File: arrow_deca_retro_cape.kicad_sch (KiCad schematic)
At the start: 74 parts, among them J1 DB15_Female_HighDensity_Mount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, J10 Conn_02x06_Odd_Even, J11 PMOD1, J12 PMOD2, J14 Conn_01x02, J15 Conn_01x03, J16 Conn_01x06, J17 Conn_01x02, J18 Conn_01x03, J19 DINC_MIN_TM_6_1, J20 PMOD3, J21 USB3_A, J22 Conn_01x03, J3 Conn_01x06, J4 DB9_Male_MountingHoles, J5 DINC_MIN_TM_6_1, J6 Conn_02x20_Odd_Even, J7 Conn_01x03, J8 P8_Male, J9 P9_Male, U4 LM1117-3.3, U5 LM1117-2.5

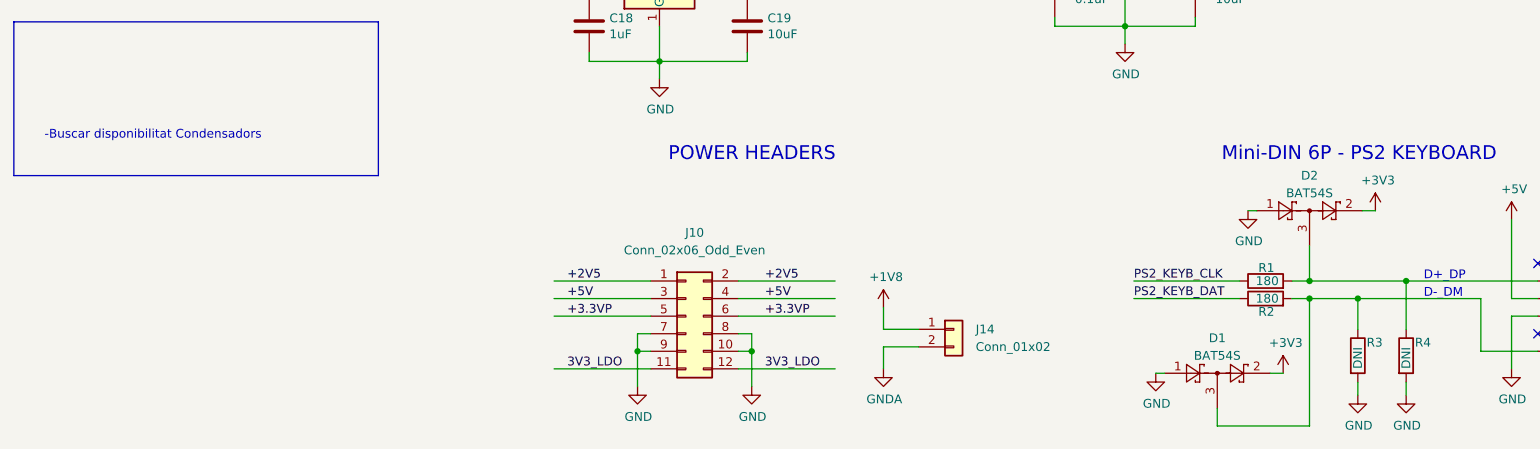
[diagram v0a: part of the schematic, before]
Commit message: updated status. received pcb. started testing
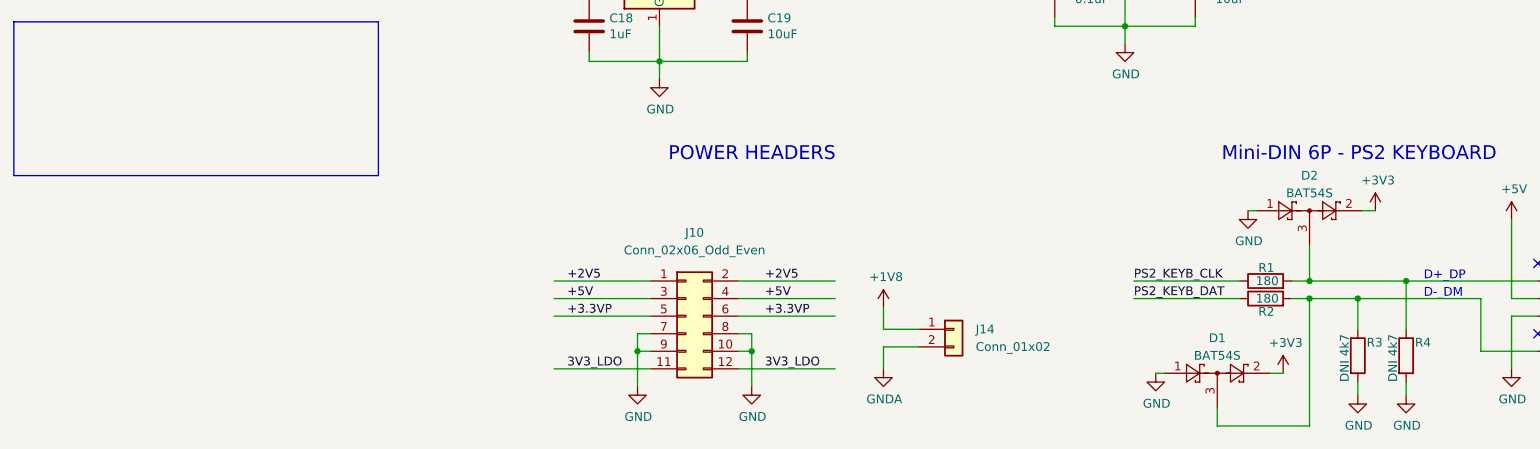
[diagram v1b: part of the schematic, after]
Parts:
- R3, R4: value DNI -> DNI 4k7
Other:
- note removed: "-Buscar disponibilitat Condensadors"
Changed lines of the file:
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@@
     (effects (font (size 2 2)) (justify left bottom))
   )
-  (text "-Buscar disponibilitat Condensadors\n" (at -52.705 240.03 0)
-    (effects (font (size 1.27 1.27)) (justify left bottom))
-  )
   (text "DETO PMOD (6 pin)" (at 33.02 151.765 0)
     (effects (font (size 2 2)) (justify left bottom))
@@
       (effects (font (size 1.27 1.27)) (justify left))
     )
-    (property "Value" "DNI" (id 1) (at 144.145 273.05 90)
+    (property "Value" "DNI 4k7" (id 1) (at 142.24 274.955 90)
       (effects (font (size 1.27 1.27)) (justify left))
     )
@@
       (effects (font (size 1.27 1.27)) (justify left))
     )
-    (property "Value" "DNI" (id 1) (at 137.16 273.05 90)
+    (property "Value" "DNI 4k7" (id 1) (at 135.255 274.955 90)
       (effects (font (size 1.27 1.27)) (justify left))
     )
@@
     )
     (path "/4e409b81-c5d2-42ba-af6f-8fc2e29e95fa"
-      (reference "R3") (unit 1) (value "DNI") (footprint "Resistor_SMD:R_0805_2012Metric_Pad1.20x1.40mm_HandSolder")
+      (reference "R3") (unit 1) (value "DNI 4k7") (footprint "Resistor_SMD:R_0805_2012Metric_Pad1.20x1.40mm_HandSolder")
     )
     (path "/1eb0fb7c-0c77-4e19-890a-f328471d6c6d"
-      (reference "R4") (unit 1) (value "DNI") (footprint "Resistor_SMD:R_0805_2012Metric_Pad1.20x1.40mm_HandSolder")
+      (reference "R4") (unit 1) (value "DNI 4k7") (footprint "Resistor_SMD:R_0805_2012Metric_Pad1.20x1.40mm_HandSolder")
     )
     (path "/9167d64e-691b-49d2-aa0b-617b235bc81c"

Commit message: v0.72 updated readme and pinout spreadsheet
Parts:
- removed J3: Conn_01x06, Connector_PinHeader_2.54mm:PinHeader_1x06_P2.54mm_Vertical, symbol Connector_Generic:Conn_01x06
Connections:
- net JOY_MUX_DETO3 renamed DETO3_JOY_MUX
- net SPI_CS_FPGA renamed SPI_CS2
- net SPI_CS_IO renamed SPI_CS1
- net SPI_CS_OSD renamed SPI_CS0_CLKBD
- net SPI_DI (MISO) renamed SPI_MISO_WSDB
- net SPI_DO (MOSI) renamed SPI_MOSI
- net SPI_SCK renamed SPI_SCLK_DABD
- no-connect marks 10 -> 9
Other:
- note added: "(DI)"
- note added: "(DO)"
- note removed: "3V3"
- note removed: "JTAG (Pogo pins)"
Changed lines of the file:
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@@
   (no_connect (at 222.885 173.355))
   (no_connect (at 222.885 158.115))
-  (no_connect (at 95.25 163.195))
   (no_connect (at 163.195 257.81))
   (no_connect (at 257.175 267.97))
@@
     (stroke (width 0) (type default) (color 0 0 0 0))
   )
-  (wire (pts (xy 95.25 165.735) (xy 78.74 165.735))
-    (stroke (width 0) (type default) (color 0 0 0 0))
-  )
   (wire (pts (xy 173.355 193.675) (xy 181.61 193.675))
     (stroke (width 0) (type default) (color 0 0 0 0))
@@
     (stroke (width 0) (type default) (color 0 0 0 0))
   )
-  (wire (pts (xy 95.25 168.275) (xy 78.74 168.275))
-    (stroke (width 0) (type default) (color 0 0 0 0))
-  )
   (wire (pts (xy 378.46 63.5) (xy 361.95 63.5))
     (stroke (width 0) (type default) (color 0 0 0 0))
@@
     (stroke (width 0) (type default) (color 0 0 0 0))
   )
-  (wire (pts (xy 95.25 173.355) (xy 78.74 173.355))
-    (stroke (width 0) (type default) (color 0 0 0 0))
-  )
   (wire (pts (xy 36.195 223.52) (xy 36.195 228.6))
     (stroke (width 0) (type default) (color 0 0 0 0))
@@
     (stroke (width 0) (type default) (color 0 0 0 0))
   )
-  (wire (pts (xy 91.44 179.07) (xy 91.44 175.895))
-    (stroke (width 0) (type default) (color 0 0 0 0))
-  )
   (wire (pts (xy 47.625 273.05) (xy 61.595 273.05))
     (stroke (width 0) (type default) (color 0 0 0 0))
@@
     (stroke (width 0) (type default) (color 0 0 0 0))
   )
-  (wire (pts (xy 95.25 170.815) (xy 78.74 170.815))
-    (stroke (width 0) (type default) (color 0 0 0 0))
-  )
   (wire (pts (xy 132.08 42.545) (xy 115.57 42.545))
     (stroke (width 0) (type default) (color 0 0 0 0))
@@
     (stroke (width 0) (type default) (color 0 0 0 0))
   )
-  (wire (pts (xy 91.44 175.895) (xy 95.25 175.895))
-    (stroke (width 0) (type default) (color 0 0 0 0))
-  )
   (wire (pts (xy 346.075 193.675) (xy 361.95 193.675))
     (stroke (width 0) (type default) (color 0 0 0 0))
@@
     (effects (font (size 1.27 1.27)) (justify left bottom))
   )
-  (text "JTAG (Pogo pins)" (at 81.915 151.765 0)
-    (effects (font (size 2 2)) (justify left bottom))
-  )
   (text "POWER HEADERS" (at 37.465 243.205 0)
     (effects (font (size 2 2)) (justify left bottom))
@@
     (effects (font (size 2 2)) (justify left bottom))
   )
-  (text "3V3" (at 88.9 163.83 0)
-    (effects (font (size 1.27 1.27)) (justify left bottom))
-  )
   (text "LRCLK" (at 25.4 169.545 0)
     (effects (font (size 1.27 1.27)) (justify left bottom))
@@
     (effects (font (size 2 2)) (justify left bottom))
   )
+  (text "(DI)" (at 228.6 93.345 0)
+    (effects (font (size 1.27 1.27)) (justify left bottom))
+  )
   (text "AIN0" (at 31.75 85.725 0)
     (effects (font (size 1.27 1.27)) (justify left bottom))
@@
     (effects (font (size 2 2)) (justify left bottom))
   )
+  (text "(DO)" (at 228.6 90.805 0)
+    (effects (font (size 1.27 1.27)) (justify left bottom))
+  )
   (text "EXTERNAL MISTER MODULE" (at 336.55 21.59 0)
     (effects (font (size 2 2)) (justify left bottom))
@@
     (effects (font (size 1.27 1.27)) (justify left bottom))
   )
-  (label "SPI_DI (MISO)" (at 38.1 73.025 0)
+  (label "SPI_MISO_WSDB" (at 38.1 73.025 0)
     (effects (font (size 1.27 1.27)) (justify left bottom))
   )
@@
     (effects (font (size 1.27 1.27)) (justify left bottom))
   )
-  (label "TMS" (at 78.74 168.275 0)
-    (effects (font (size 1.27 1.27)) (justify left bottom))
-  )
   (label "DQ6" (at 118.11 50.165 0)
     (effects (font (size 1.27 1.27)) (justify left bottom))
@@
     (effects (font (size 1.27 1.27)) (justify left bottom))
   )
-  (label "JOY_MUX_DETO3" (at 255.905 203.835 0)
+  (label "DETO3_JOY_MUX" (at 255.905 203.835 0)
     (effects (font (size 1.27 1.27)) (justify left bottom))
   )
@@
     (effects (font (size 1.27 1.27)) (justify left bottom))
   )
-  (label "SPI_CS_IO" (at 153.67 40.005 0)
+  (label "SPI_CS1" (at 153.67 40.005 0)
     (effects (font (size 1.27 1.27)) (justify left bottom))
   )
-  (label "JOY_MUX_DETO3" (at 38.1 88.265 0)
+  (label "DETO3_JOY_MUX" (at 38.1 88.265 0)
     (effects (font (size 1.27 1.27)) (justify left bottom))
   )
@@
     (effects (font (size 1.27 1.27)) (justify left bottom))
   )
-  (label "JOY_MUX_DETO3" (at 32.385 167.005 0)
+  (label "DETO3_JOY_MUX" (at 32.385 167.005 0)
     (effects (font (size 1.27 1.27)) (justify left bottom))
   )
@@
     (effects (font (size 1.27 1.27)) (justify left bottom))
   )
-  (label "TDI" (at 78.74 165.735 0)
-    (effects (font (size 1.27 1.27)) (justify left bottom))
-  )
   (label "A7" (at 336.55 58.42 0)
     (effects (font (size 1.27 1.27)) (justify left bottom))
@@
     (effects (font (size 1.27 1.27)) (justify left bottom))
   )
-  (label "SPI_CS_OSD" (at 217.805 88.265 0)
+  (label "SPI_CS0_CLKBD" (at 213.36 88.265 0)
     (effects (font (size 1.27 1.27)) (justify left bottom))
   )
@@
     (effects (font (size 1.27 1.27)) (justify left bottom))
   )
-  (label "SPI_CS_IO" (at 254.635 93.345 0)
+  (label "SPI_CS1" (at 254.635 93.345 0)
     (effects (font (size 1.27 1.27)) (justify left bottom))
   )
@@
     (effects (font (size 1.27 1.27)) (justify left bottom))
   )
-  (label "SPI_DO (MOSI)" (at 68.58 73.025 0)
+  (label "SPI_MOSI" (at 68.58 73.025 0)
     (effects (font (size 1.27 1.27)) (justify left bottom))
   )
-  (label "SPI_DO (MOSI)" (at 217.805 90.805 0)
+  (label "SPI_MOSI" (at 213.36 90.805 0)
     (effects (font (size 1.27 1.27)) (justify left bottom))
   )
@@
     (effects (font (size 1.27 1.27)) (justify left bottom))
   )
-  (label "SPI_SCK" (at 217.805 95.885 0)
+  (label "SPI_SCLK_DABD" (at 213.36 95.885 0)
     (effects (font (size 1.27 1.27)) (justify left bottom))
   )
@@
     (effects (font (size 1.27 1.27)) (justify left bottom))
   )
-  (label "SPI_CS_OSD" (at 118.11 40.005 0)
+  (label "SPI_CS0_CLKBD" (at 118.11 40.005 0)
     (effects (font (size 1.27 1.27)) (justify left bottom))
   )
@@
     (effects (font (size 1.27 1.27)) (justify left bottom))
   )
-  (label "TDO" (at 78.74 170.815 0)
-    (effects (font (size 1.27 1.27)) (justify left bottom))
-  )
   (label "DQ8" (at 153.67 62.865 0)
     (effects (font (size 1.27 1.27)) (justify left bottom))
@@
     (effects (font (size 1.27 1.27)) (justify left bottom))
   )
-  (label "SPI_DI (MISO)" (at 217.805 93.345 0)
+  (label "SPI_MISO_WSDB" (at 213.36 93.345 0)
     (effects (font (size 1.27 1.27)) (justify left bottom))
   )
@@
     (effects (font (size 1.27 1.27)) (justify left bottom))
   )
-  (label "SPI_CS_FPGA" (at 68.58 88.265 0)
+  (label "SPI_CS2" (at 68.58 88.265 0)
     (effects (font (size 1.27 1.27)) (justify left bottom))
   )
@@
     (effects (font (size 1.27 1.27)) (justify left bottom))
   )
-  (label "TCK" (at 78.74 173.355 0)
-    (effects (font (size 1.27 1.27)) (justify left bottom))
-  )
-  (label "SPI_CS_FPGA" (at 254.635 95.885 0)
+  (label "SPI_CS2" (at 254.635 95.885 0)
     (effects (font (size 1.27 1.27)) (justify left bottom))
   )
@@
     (effects (font (size 1.27 1.27)) (justify left bottom))
   )
-  (label "SPI_SCK" (at 38.1 75.565 0)
+  (label "SPI_SCLK_DABD" (at 38.1 75.565 0)
     (effects (font (size 1.27 1.27)) (justify left bottom))
   )
@@
     (pin "3")
   )
-  (symbol (lib_id "power:GND") (at 91.44 179.07 0) (unit 1)
-    (in_bom yes) (on_board yes)
-    (property "Reference" "#PWR02" (id 0) (at 91.44 185.42 0)
-      (effects (font (size 1.27 1.27)) hide)
-    )
-    (property "Value" "GND" (id 1) (at 91.567 183.4642 0))
-    (property "Footprint" "" (id 2) (at 91.44 179.07 0)
-      (effects (font (size 1.27 1.27)) hide)
-    )
-    (property "Datasheet" "" (id 3) (at 91.44 179.07 0)
-      (effects (font (size 1.27 1.27)) hide)
-    )
-    (pin "1")
-  )
   (symbol (lib_id "Device:C") (at 113.665 218.44 0) (unit 1)
     (in_bom yes) (on_board yes)
@@
     (pin "9")
   )
-  (symbol (lib_id "Connector_Generic:Conn_01x06") (at 100.33 168.275 0) (unit 1)
-    (in_bom yes) (on_board yes) (fields_autoplaced)
-    (property "Reference" "J3" (id 0) (at 102.87 168.2749 0)
-      (effects (font (size 1.27 1.27)) (justify left))
-    )
-    (property "Value" "Conn_01x06" (id 1) (at 102.87 170.8149 0)
-      (effects (font (size 1.27 1.27)) (justify left))
-    )
-    (property "Footprint" "Connector_PinHeader_2.54mm:PinHeader_1x06_P2.54mm_Vertical" (id 2) (at 100.33 168.275 0)
-      (effects (font (size 1.27 1.27)) hide)
-    )
-    (property "Datasheet" "~" (id 3) (at 100.33 168.275 0)
-      (effects (font (size 1.27 1.27)) hide)
-    )
-    (pin "1")
-    (pin "2")
-    (pin "3")
-    (pin "4")
-    (pin "5")
-    (pin "6")
-  )
   (symbol (lib_id "Device:R") (at 169.545 149.225 90) (unit 1)
     (in_bom yes) (on_board yes)
@@
       (reference "#PWR01") (unit 1) (value "GND") (footprint "")
     )
-    (path "/aaab055d-e2c8-47ec-bf52-ba6cbf89c068"
-      (reference "#PWR02") (unit 1) (value "GND") (footprint "")
-    )
     (path "/2536e930-06a4-43c1-bb06-fbe9f6f63e41"
       (reference "#PWR03") (unit 1) (value "GND") (footprint "")
@@
       (reference "J1") (unit 1) (value "DB15_Female_HighDensity_MountingHoles") (footprint "vga:DSUB-15-HD_Female_Horizontal_P2.29x2.54mm_EdgePinOffset3.03mm_Housed_MountingHolesOffset4.94mm")
     )
-    (path "/e9a4ad61-c16f-4a36-9385-12858092576f"
-      (reference "J3") (unit 1) (value "Conn_01x06") (footprint "Connector_PinHeader_2.54mm:PinHeader_1x06_P2.54mm_Vertical")
-    )
     (path "/5d157a0f-3ba8-4d7f-8aff-9786af9f14a7"

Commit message: v0.75 see changelog
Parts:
- removed D1, D10, D11, D12, D2, D3, D4, D5, D6, D7, D8, D9: BAT54S, Package_TO_SOT_SMD:SOT-23, symbol Diode:BAT54S
- added D1, D12, D2, D3, D4: MMSZ5225BG, Diode_SMD:D_SOD-123, symbol Diode:BZT52Bxx
- added D10, D11, D5, D6, D7, D8, D9: MMSZ5221BT1G, Diode_SMD:D_SOD-123, symbol Diode:BZT52Bxx
- added JP3: (no value), symbol Jumper:SolderJumper_2_Open
- added JP4: Conn_01x02, Connector_PinHeader_2.54mm:PinHeader_1x02_P2.54mm_Vertical, symbol Connector_Generic:Conn_01x02
- J1: footprint vga:DSUB-15-HD_Female_Horizontal_P2.29x2.54mm_EdgePinOffset3.03mm_Housed_MountingHolesOffset4.94mm -> Connector_Dsub:DSUB-15-HD_Female_Horizontal_P2.29x1.98mm_EdgePinOffset3.03mm_Housed_MountingHolesOffset4.94mm
- J10: footprint Connector_PinSocket_2.54mm:PinSocket_2x06_P2.54mm_Vertical -> Connector_PinSocket_2.54mm:PinSocket_1x06_P2.54mm_Vertical; symbol Connector_Generic:Conn_02x06_Odd_Even -> Connector_Generic:Conn_01x06
- J16: footprint Connector_PinHeader_2.54mm:PinHeader_1x06_P2.54mm_Vertical -> Connector_PinSocket_2.54mm:PinSocket_1x06_P2.54mm_Vertical
- R1, R10, R11, R12, R13, R14, R15, R16, R2, R5, R6, R9: value 180 -> 510
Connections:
- net +2V5: no longer J10.2 (Pin_2)
- net +3.3VP: now also J10.4 (Pin_4); no longer J10.5 (Pin_5), J10.6 (Pin_6)
- net +5V: now also J10.2 (Pin_2), JP4.2 (Pin_2); no longer J10.3 (Pin_3), J10.4 (Pin_4)
- net 3V3_LDO: now also J10.6 (Pin_6); no longer J10.11 (Pin_11), J10.12 (Pin_12)
- net GND: now also J10.3 (Pin_3), J10.5 (Pin_5), D1.2 (A), D10.2 (A), D11.2 (A), D12.2 (A), D2.2 (A), D3.2 (A), D4.2 (A), D5.2 (A), D6.2 (A), D7.2 (A), D8.2 (A), D9.2 (A); no longer J10.10 (Pin_10), J10.7 (Pin_7), J10.8 (Pin_8), J10.9 (Pin_9)
- net JOY1_B1_P6: now also D8.1 (K)
- net JOY1_B2_P9: now also D5.1 (K)
- net JOY1_DOWN: now also D6.1 (K)
- net JOY1_LEFT: now also D9.1 (K)
- net JOY1_RIGHT: now also D7.1 (K)
- net JOY1_UP: now also D10.1 (K)
- net MUX: now also JP3.2 (B); no longer R16.2
- net PS2_KEYB_CLK: now also D1.1 (K)
- net PS2_KEYB_DAT: now also D2.1 (K)
- net PS2_MOUSE_CLK: now also D3.1 (K)
- net PS2_MOUSE_DAT: now also D4.1 (K)
- net at J1.9: now also JP4.1 (Pin_1)
- new net: JP3.1 (A), R16.2
- no-connect marks 9 -> 8
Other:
- note added: "DNI"
- moved on the sheet: C18, C19, C20, C21, J1, J12, J14, J15, J16, J18, J19, J20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

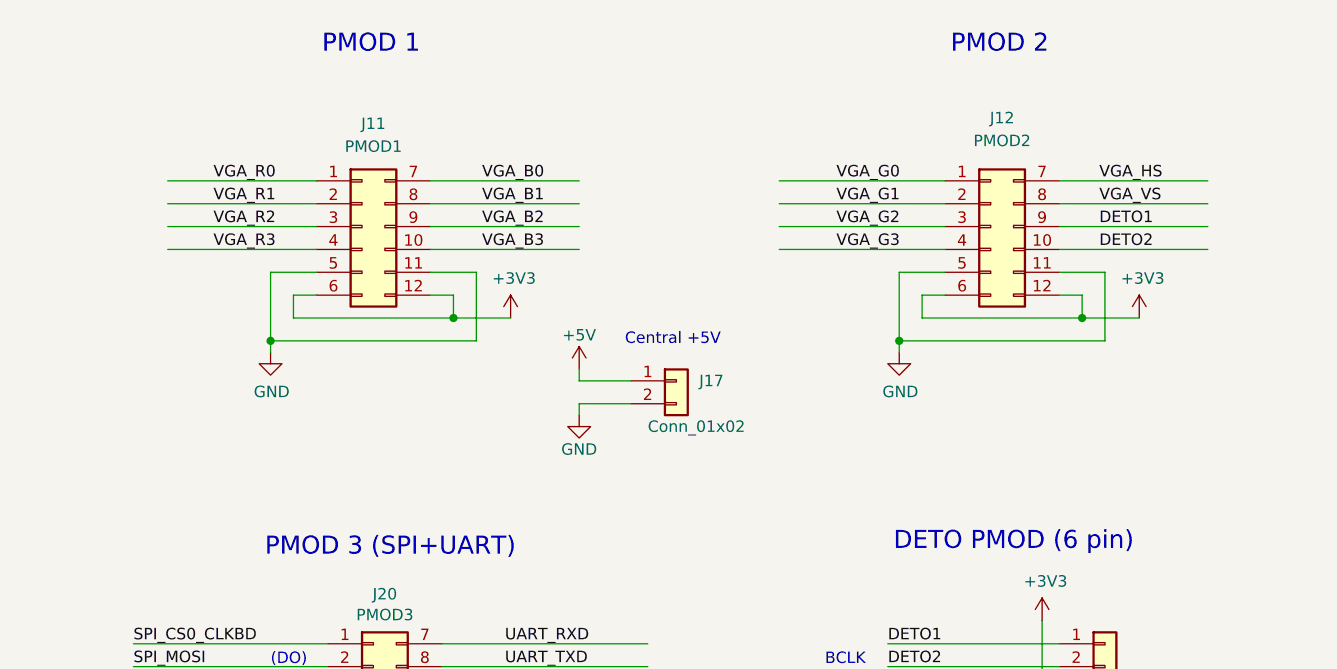
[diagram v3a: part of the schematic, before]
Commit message: v0.76 double pmod added 4 central pins
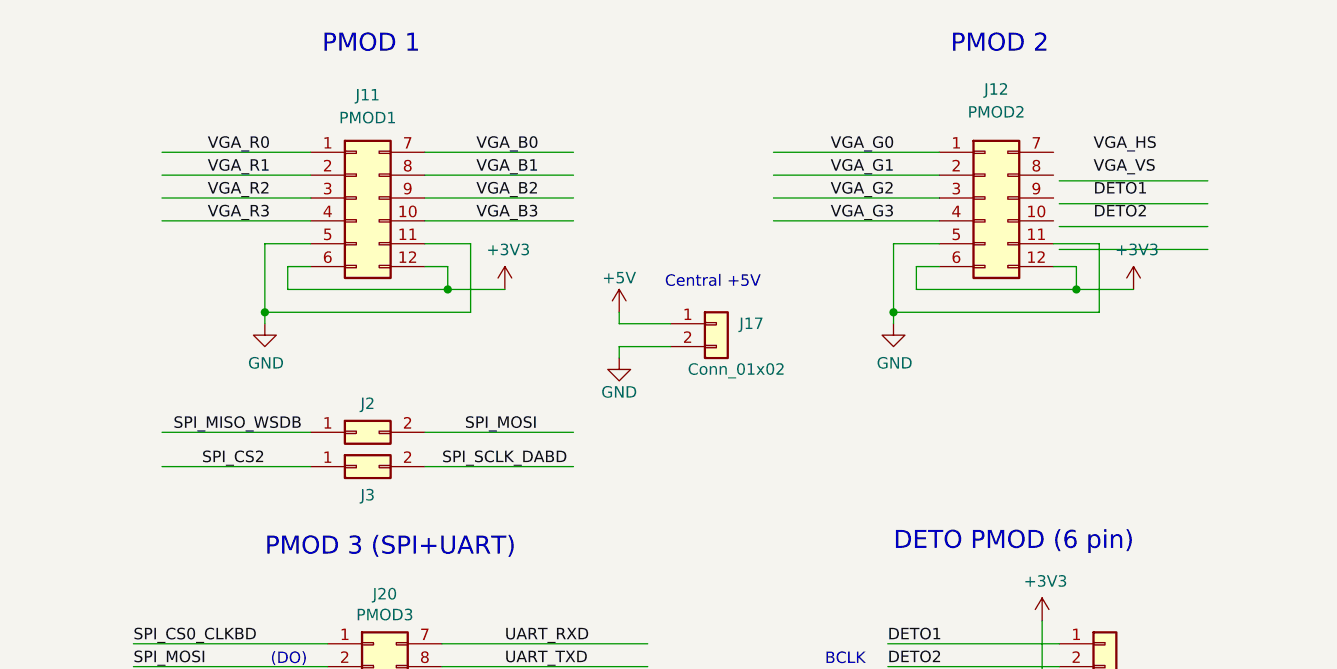
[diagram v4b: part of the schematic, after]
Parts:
- added J2, J3: (no value), symbol Connector_Generic:Conn_02x01
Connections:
- net DETO1: no longer J12.9 (Pin_9)
- net DETO2: no longer J12.10 (Pin_10)
- net SPI_CS2: now also J3.1 (Pin_1)
- net SPI_MISO_WSDB: now also J2.1 (Pin_1)
- net SPI_MOSI: now also J2.2 (Pin_2)
- net SPI_SCLK_DABD: now also J3.2 (Pin_2)
- net VGA_HS: no longer J12.7 (Pin_7)
- net VGA_VS: no longer J12.8 (Pin_8)
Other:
- moved on the sheet: J11, J12, J17

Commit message: v0.77 see changelog
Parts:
- removed JP2: Conn_01x03, Connector_PinHeader_2.54mm:PinHeader_1x03_P2.54mm_Vertical, symbol Connector_Generic:Conn_01x03
- added JP2, JP7: SolderJumper_3_Open, Jumper:SolderJumper-3_P2.0mm_Open_TrianglePad1.0x1.5mm, symbol Jumper:SolderJumper_3_Open
- added JP5, JP6: Conn_01x02, Connector_PinHeader_2.54mm:PinHeader_1x02_P2.54mm_Vertical, symbol Connector_Generic:Conn_01x02
- J2, J3: value (none) -> Conn_02x01; footprint (none) -> Connector_PinSocket_2.54mm:PinSocket_1x02_P2.54mm_Vertical
- JP3: value (none) -> SolderJumper_2_Open; footprint (none) -> Jumper:SolderJumper-2_P1.3mm_Open_RoundedPad1.0x1.5mm
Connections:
- net +2V5: now also JP7.3 (B)
- net +3.3VP: now also J10.3 (Pin_3), JP2.1 (A); no longer J10.4 (Pin_4)
- net +3V3: now also JP2.2 (C), JP6.1 (Pin_1); no longer J6.29 (Pin_29)
- net +5V: now also JP5.1 (Pin_1), JP7.1 (A); no longer J4.5, J6.11 (Pin_11)
- net 3V3_LDO: now also JP2.3 (B)
- net GND: now also J10.4 (Pin_4); no longer J10.3 (Pin_3)
- new net: J6.29 (Pin_29), JP6.2 (Pin_2)
- new net: J6.11 (Pin_11), JP5.2 (Pin_2)
- new net +JOY_PWR: J4.5, JP7.2 (C)
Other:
- moved on the sheet: C18, C19, C20, C21, J10, J14, J15, R17, R18, U4, U5
